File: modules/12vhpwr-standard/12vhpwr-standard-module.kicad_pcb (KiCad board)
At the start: 4 copper layers, 58 x 80 mm, 80 parts, among them J1 TO-HUB, J3 12V-2x6 IN, J4 12V-2x6 OUT pigtail, J5 USB-C 2.0, SW1 BOOT, SW2 RESET, U1 ESP32-S3-MINI-1-N4R2, U10 INA240A3, U11 INA240A3, U12 INA240A3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

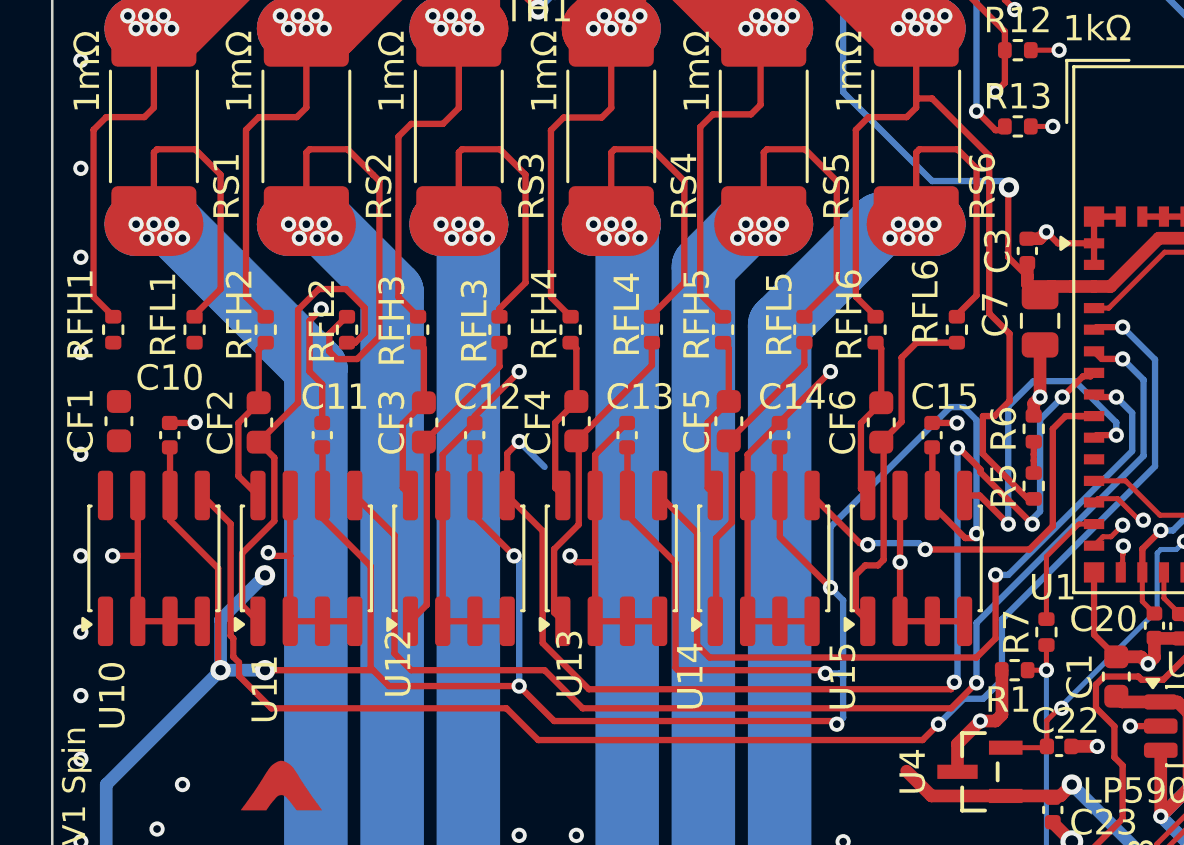
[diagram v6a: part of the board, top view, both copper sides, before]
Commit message: Routed INPP as pairs.
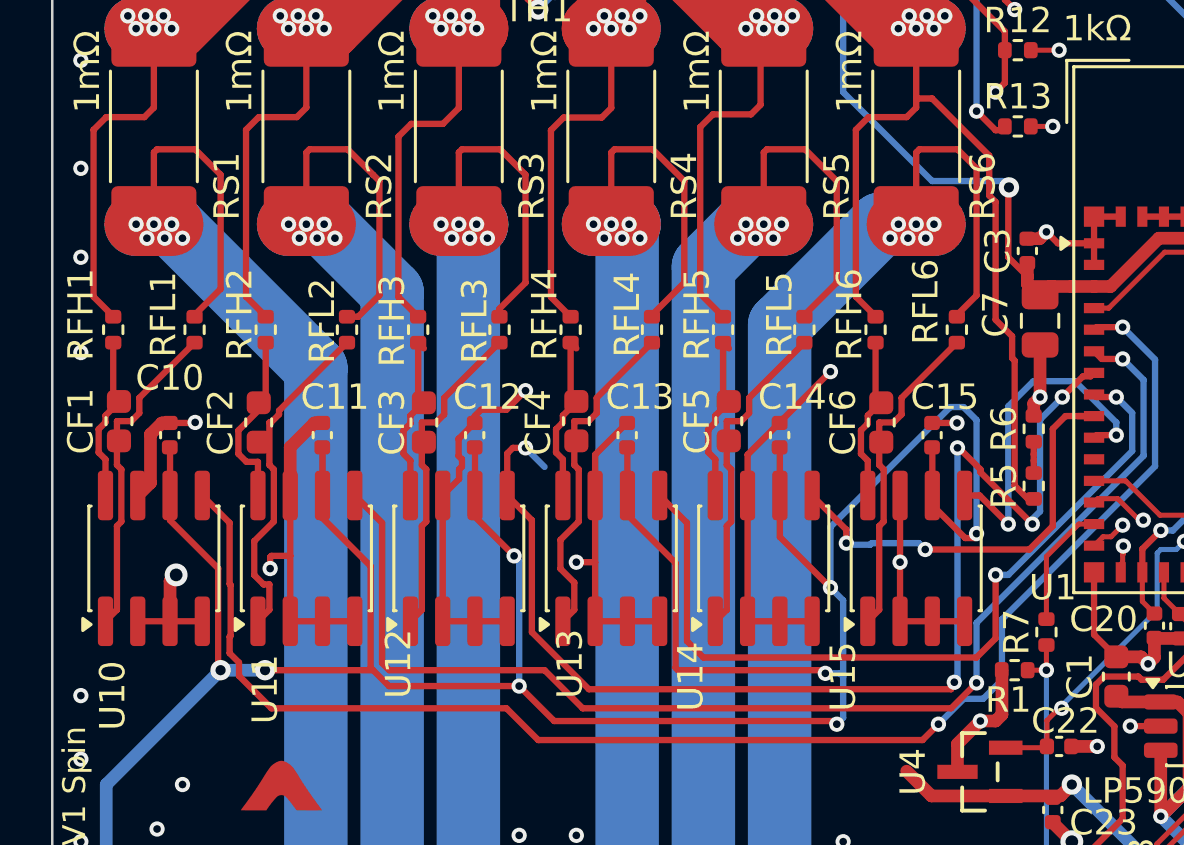
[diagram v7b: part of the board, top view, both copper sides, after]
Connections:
- net /INNP1 renamed /IN1_N
- net /INNP2 renamed /IN2_N
- net /INNP3 renamed /IN3_N
- net /INNP4 renamed /IN4_N
- net /INNP5 renamed /IN5_N
- net /INNP6 renamed /IN6_N
- net /INPP1 renamed /IN1_P
- net /INPP2 renamed /IN2_P
- net /INPP3 renamed /IN3_P
- net /INPP4 renamed /IN4_P
- net /INPP5 renamed /IN5_P
- net /INPP6 renamed /IN6_P
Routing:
- net /IN1_N: track 0.19 -> 13.1 mm
- net /IN1_P: track 0.00 -> 6.37 mm
- net /IN2_N: track 19.1 -> 13.2 mm
- net +3V3: track 247.5 -> 243.0 mm, vias 22 -> 21
- net /SENSEP2_LO: track 73.3 -> 69.2 mm
- net GND: track 168.9 -> 167.2 mm, vias 214 -> 210
- net /IN6_N: track 14.1 -> 12.9 mm
- net /SENSEP6_HI: track 57.3 -> 56.2 mm
- net /IN4_N: track 13.2 -> 13.7 mm
- net /ISENSEP2: track 48.1 -> 48.7 mm

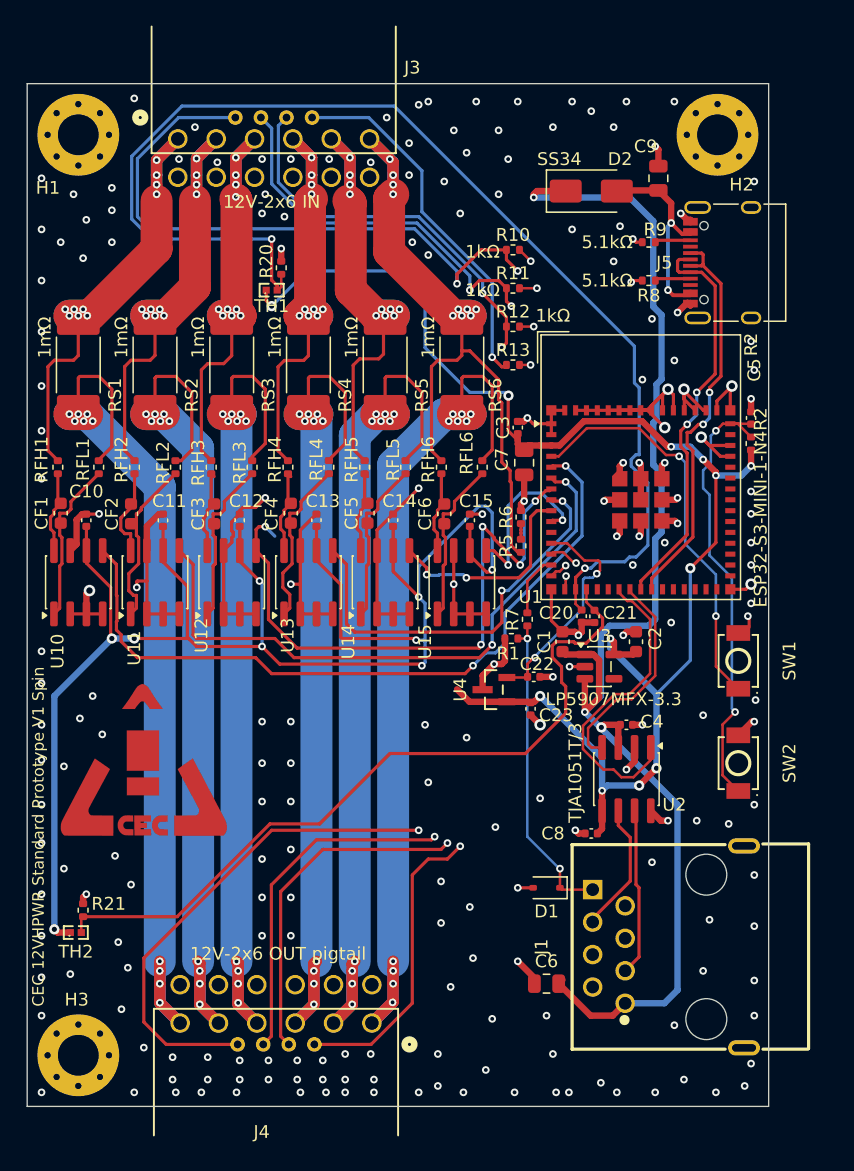
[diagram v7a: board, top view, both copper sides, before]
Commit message: Finished sideband routing.
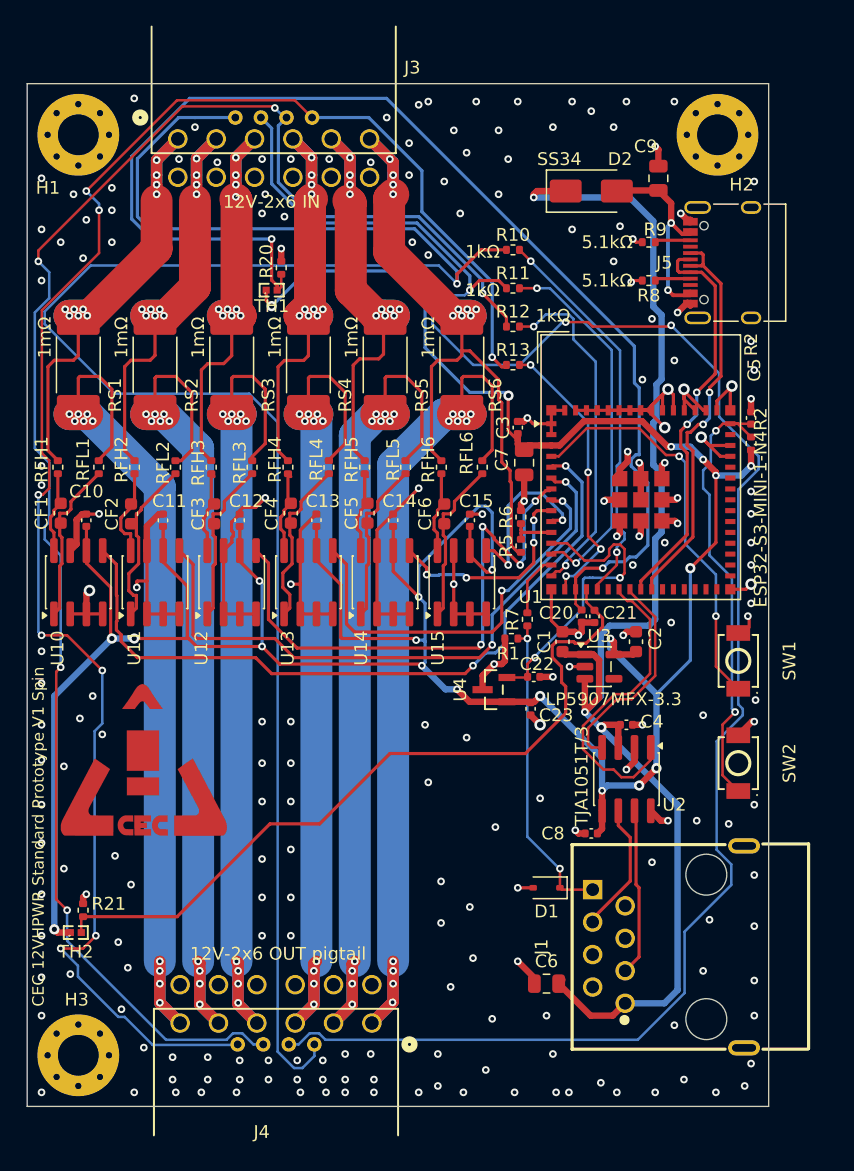
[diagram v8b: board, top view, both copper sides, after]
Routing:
- net /SB_SENSE1: track 56.9 -> 146.7 mm
- net /SB_SENSE0: track 72.4 -> 157.3 mm, vias 3 -> 1
- net /SB_PWR_STABLE: track 57.7 -> 128.9 mm, vias 3 -> 5
- net /SB_CBL_PRES: track 67.4 -> 135.3 mm, vias 2 -> 8
- net /SB_SENSE0_GPIO: track 1.25 -> 31.0 mm, vias 1 -> 2
- net /SB_SENSE1_GPIO: track 3.71 -> 29.4 mm
- net /SB_PWR_STABLE_GPIO: track 2.57 -> 27.2 mm
- net /SB_CBL_PRES_GPIO: track 1.94 -> 22.2 mm, vias 2 -> 4
- net /VREF: track 17.8 -> 23.7 mm
- net /ISENSEP3: track 47.7 -> 44.2 mm, vias 5 -> 4
- net +3V3: track 243.0 -> 246.5 mm, vias 21 -> 22
- net /VRAIL_DIV: track 1.23 -> 3.63 mm
- net GND: track 167.2 -> 168.2 mm, vias 210 -> 208
- net /ISENSEP5: track 17.5 -> 16.9 mm, vias 2 -> 4
